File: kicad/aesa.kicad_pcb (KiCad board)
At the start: 4 copper layers, 192 x 301 mm, 2132 parts, among them J9501 12 V in (5.5x2.1), J9502 TX power (shunt), J9901 EX_IO1 (AXU3EGB J15), J9902 EX_IO2 (AXU3EGB J16), U1001 OPA1678IDR, U101 OPA1678IDR, U10101 74HCT595D, U10102 UCC27524DR, U10103 UCC27524DR, U10201 74HCT595D, U10202 UCC27524DR, U10203 UCC27524DR, U10301 74HCT595D, U10302 UCC27524DR, U10303 UCC27524DR, U10401 74HCT595D, U10402 UCC27524DR, U10403 UCC27524DR, U10501 74HCT595D, U10502 UCC27524DR, U10503 UCC27524DR, U10601 74HCT595D, U10602 UCC27524DR, U10603 UCC27524DR, U10701 74HCT595D, U10702 UCC27524DR, U10703 UCC27524DR, U10801 74HCT595D, U10802 UCC27524DR, U10803 UCC27524DR, U10901 74HCT595D, U10902 UCC27524DR, U10903 UCC27524DR, U11001 74HCT595D, U11002 UCC27524DR, U11003 UCC27524DR, U1101 OPA1678IDR, U11101 74HCT595D, U11102 UCC27524DR, U11103 UCC27524DR, U11201 74HCT595D, U11202 UCC27524DR, U11203 UCC27524DR, U11301 74HCT595D, U11302 UCC27524DR, U11303 UCC27524DR, U11401 74HCT595D, U11402 UCC27524DR, U11403 UCC27524DR, U11501 74HCT595D, U11502 UCC27524DR, U11503 UCC27524DR, U11601 74HCT595D, U11602 UCC27524DR, U11603 UCC27524DR, U1201 OPA1678IDR, U12101 74AHCT1G125, U12201 74AHCT1G125, U12301 74AHCT1G125, U12401 74AHCT1G125, U1301 OPA1678IDR, U13101 74LVC2G34, U13201 74LVC2G34, U13301 74LVC2G34, U13401 74LVC2G34, U13501 74LVC2G34, U13601 74LVC2G34, U13701 74LVC2G34, U13801 74LVC2G34, U13901 74LVC2G34, U1401 OPA1678IDR, U1501 OPA1678IDR, U1601 OPA1678IDR, U1701 OPA1678IDR, U1801 OPA1678IDR, U1901 OPA1678IDR, U2001 OPA1678IDR, U201 OPA1678IDR, U2101 OPA1678IDR, U2201 OPA1678IDR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

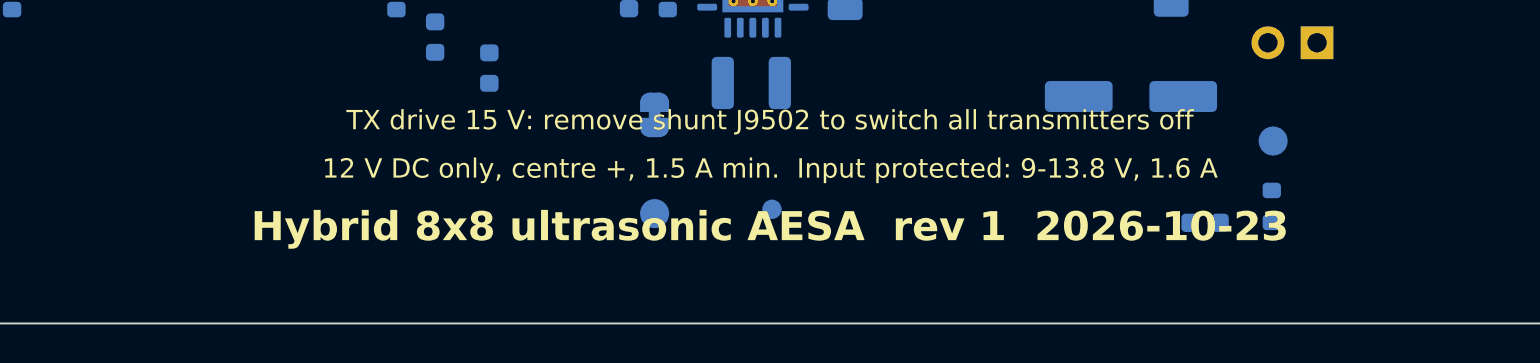
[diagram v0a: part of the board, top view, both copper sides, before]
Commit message: Fix small inconsistencies: one revision (rev 1, 2026-10-24) for sheets and board
- REV/DATE come from scripts/common.py for every title block and the board
  silkscreen (the sheets said rev 2, the board rev 1).
- Channel note: +27 dB is element -> amplifier output; the ADC pin sees
  +16.5 dB after the divider.
- Board input text 8.8-13.8 V (eFuse UVLO); LM2731 limit 14 V (14.5 V abs max).
- Brief/README: real board size 192 x 301 mm, CUSP-TR80 footprint and pitch
  note, nominal vs simulated gain, board test-point references, 126 pages.
- SKiDL spec uses L_Ferrite like the sheet; dead AD7606/net-tie entries gone.

ERC 0, DRC 0, design check 19/19, placement checks 12/12.
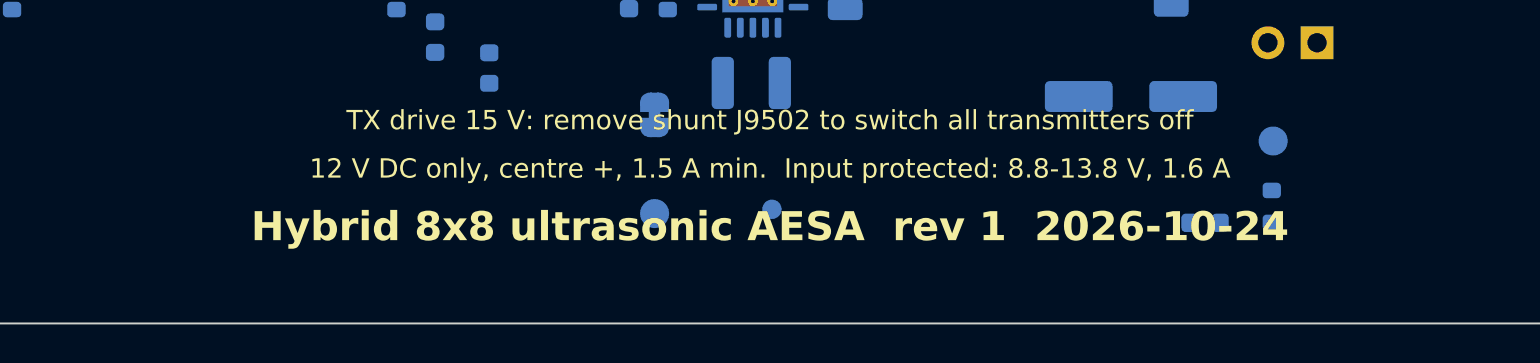
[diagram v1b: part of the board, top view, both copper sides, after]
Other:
- board text added: "12 V DC only, centre +, 1.5 A min. Input protected: 8.8-13.8 V, 1.6 A"
- board text added: "Hybrid 8x8 ultrasonic AESA rev 1 2026-10-24"
- board text removed: "12 V DC only, centre +, 1.5 A min. Input protected: 9-13.8 V, 1.6 A"
- board text removed: "Hybrid 8x8 ultrasonic AESA rev 1 2026-10-23"
